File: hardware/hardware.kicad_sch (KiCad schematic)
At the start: 8 parts, among them J1 USB_C_Receptacle_USB2.0_14P, J2 Conn_01x04_Socket, J3 Conn_01x08_Socket, J4 Conn_01x04_Socket, U1 AMS1117-3.3, U2 ESP32-S3-WROOM-1

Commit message: Update Footprint property for connectors in schematic
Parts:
- J2, J4: footprint (none) -> Connector_PinHeader_2.54mm:PinHeader_1x04_P2.54mm_Vertical
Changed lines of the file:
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@@
 			)
 		)
-		(property "Footprint" ""
+		(property "Footprint" "Connector_PinHeader_2.54mm:PinHeader_1x04_P2.54mm_Vertical"
 			(at 200.66 24.13 0)
 			(effects
@@
 			)
 		)
-		(property "Footprint" ""
+		(property "Footprint" "Connector_PinHeader_2.54mm:PinHeader_1x04_P2.54mm_Vertical"
 			(at 252.73 24.13 0)
 			(effects

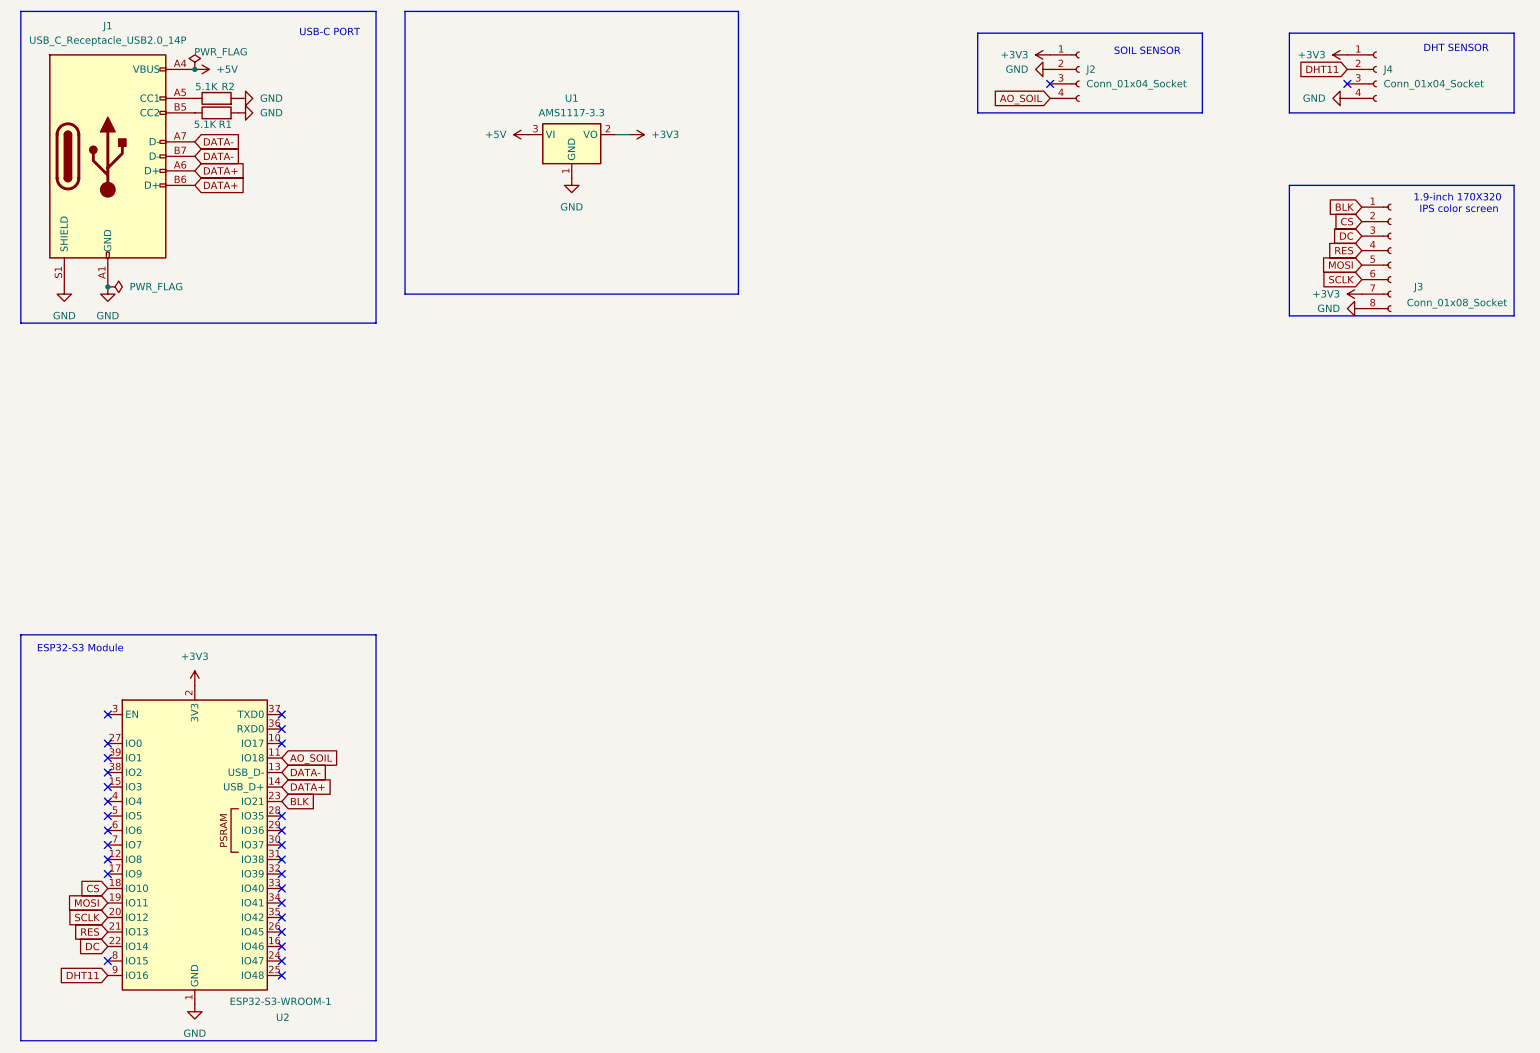
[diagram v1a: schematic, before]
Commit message: Adding Light sensor pins on schematic
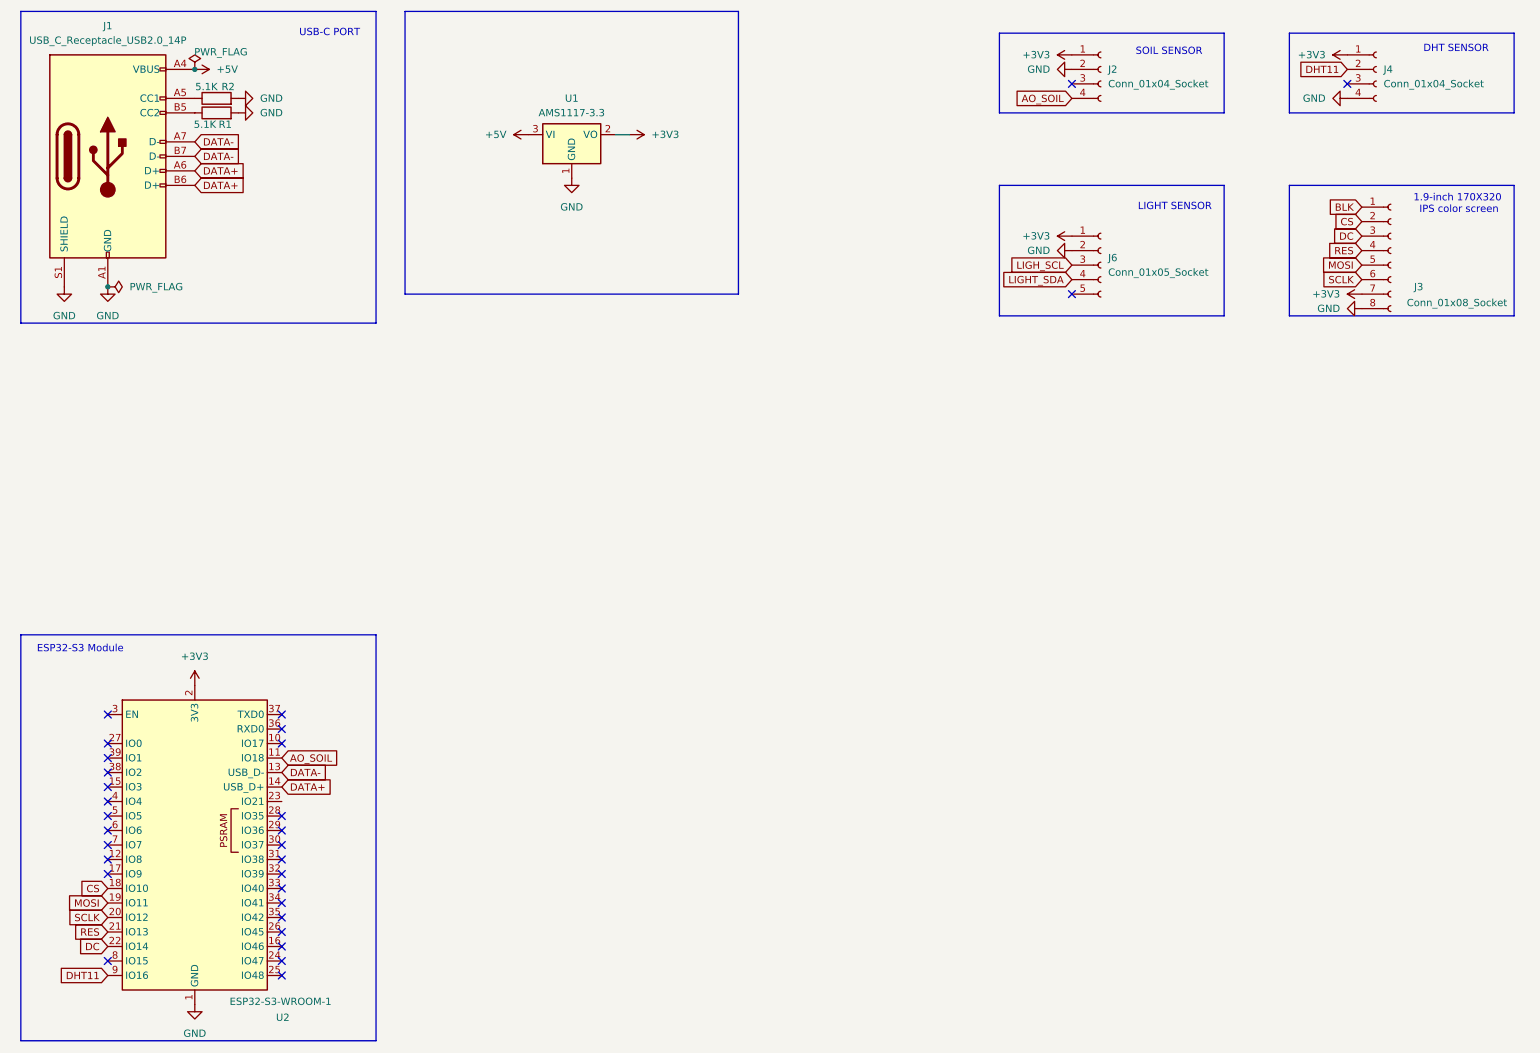
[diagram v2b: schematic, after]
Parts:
- added J6: Conn_01x05_Socket, symbol Connector:Conn_01x05_Socket
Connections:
- net +3V3: now also J6.1 (Pin_1)
- net BLK: no longer U2.23 (IO21)
- net GND: now also J6.2 (Pin_2)
- new net LIGHT_SDA: J6.4 (Pin_4)
- new net LIGH_SCL: J6.3 (Pin_3)
- no-connect marks 29 -> 30
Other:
- note added: "LIGHT SENSOR"
- moved on the sheet: J2

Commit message: Adding all capacitors
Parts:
- added C1, C2: 10uF, Capacitor_SMD:C_0805_2012Metric, symbol Device:C
- added C3, C6: 0.1uF, Capacitor_SMD:C_0805_2012Metric, symbol Device:C
- added C4, C7: 22uF, Capacitor_SMD:C_0805_2012Metric, symbol Device:C
- added C5: 10nF, Capacitor_SMD:C_0805_2012Metric, symbol Device:C
- J6: footprint (none) -> Connector_PinHeader_2.54mm:PinHeader_1x05_P2.54mm_Vertical
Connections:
- net +3V3: now also C1.2, C3.2, C4.1, C6.1, C7.1
- net +5V: now also C2.2, C5.1
- net GND: now also C1.1, C2.1, C3.1, C4.2, C5.2, C6.2, C7.2
- no-connect marks 30 -> 31
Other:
- note added: "sooit 22uF en ceramique soit 10uF en tantale"
- moved on the sheet: J1, J4, R1, R2

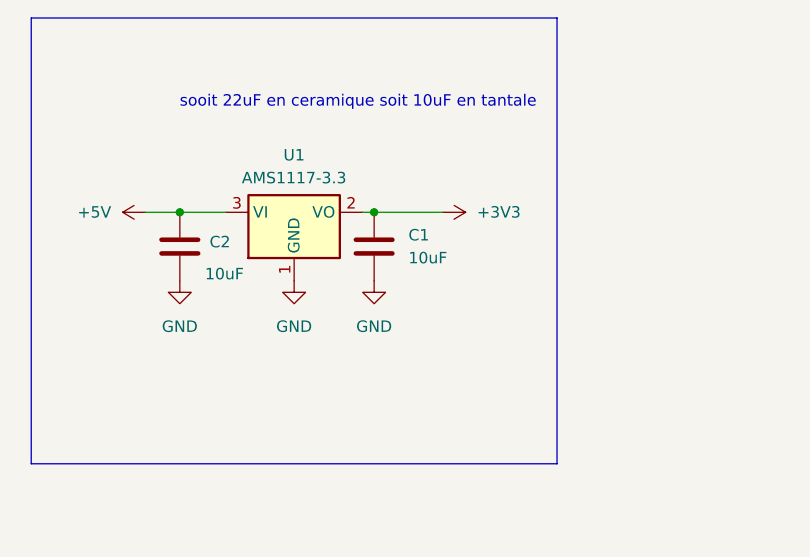
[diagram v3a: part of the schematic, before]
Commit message: Making first version of the PCB [NOT ROUTED ]
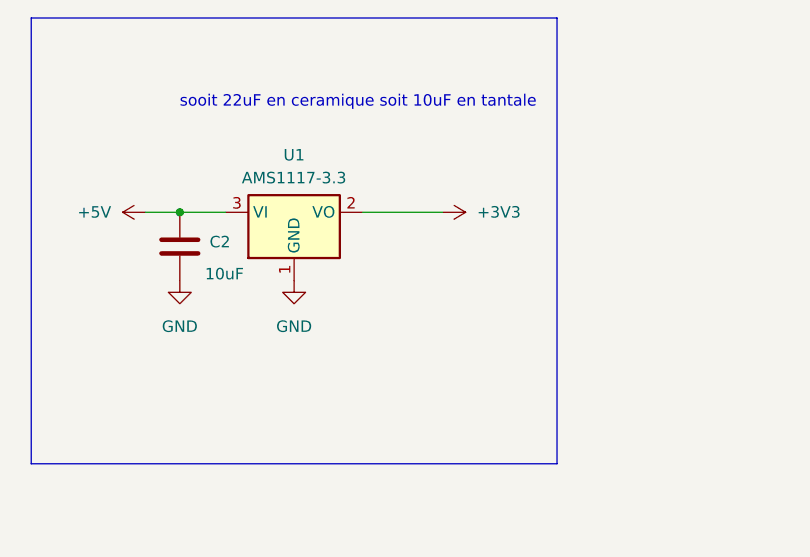
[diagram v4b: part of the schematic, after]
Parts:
- removed C1: 10uF, Capacitor_SMD:C_0805_2012Metric, symbol Device:C
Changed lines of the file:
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@@
-	)
-	(junction
-		(at 120.65 35.56)
-		(diameter 0)
-		(color 0 0 0 0)
 	)
 	(junction
@@
 	(wire
 		(pts
-			(xy 128.27 35.56) (xy 120.65 35.56)
+			(xy 55.88 29.21) (xy 46.99 29.21)
 		)
 		(stroke
@@
 	(wire
 		(pts
-			(xy 55.88 29.21) (xy 46.99 29.21)
+			(xy 45.72 130.81) (xy 45.72 132.08)
 		)
 		(stroke
@@
 	(wire
 		(pts
-			(xy 45.72 130.81) (xy 45.72 132.08)
-		)
-		(stroke
-			(width 0)
-			(type default)
-		)
-	)
-	(wire
-		(pts
-			(xy 120.65 35.56) (xy 119.38 35.56)
+			(xy 119.38 35.56) (xy 128.27 35.56)
 		)
 		(stroke
@@
 	)
 	(symbol
-		(lib_id "Device:C")
-		(at 120.65 39.37 180)
-		(unit 1)
-		(exclude_from_sim no)
-		(in_bom yes)
-		(on_board yes)
-		(dnp no)
-		(fields_autoplaced yes)
-		(property "Reference" "C1"
-			(at 124.46 38.0999 0)
-			(effects
-				(font
-					(size 1.27 1.27)
-				)
-				(justify right)
-			)
-		)
-		(property "Value" "10uF"
-			(at 124.46 40.6399 0)
-			(effects
-				(font
-					(size 1.27 1.27)
-				)
-				(justify right)
-			)
-		)
-		(property "Footprint" "Capacitor_SMD:C_0805_2012Metric"
-			(at 119.6848 35.56 0)
-			(effects
-				(font
-					(size 1.27 1.27)
-				)
-				(hide yes)
-			)
-		)
-		(property "Datasheet" "~"
-			(at 120.65 39.37 0)
-			(effects
-				(font
-					(size 1.27 1.27)
-				)
-				(hide yes)
-			)
-		)
-		(property "Description" "Unpolarized capacitor"
-			(at 120.65 39.37 0)
-			(effects
-				(font
-					(size 1.27 1.27)
-				)
-				(hide yes)
-			)
-		)
-		(pin "1"
-		)
-		(pin "2"
-		)
-		(instances
-			(project ""
-				(path "/a233d2e6-40a7-473a-8214-598adc2356c8"
-					(reference "C1")
-					(unit 1)
-				)
-			)
-		)
-	)
-	(symbol
 		(lib_id "power:GND")
 		(at 53.34 123.19 90)
@@
 					(unit 1)
 				)
-			)
-		)
-	)
-	(symbol
-		(lib_id "power:GND")
-		(at 120.65 43.18 0)
-		(unit 1)
-		(exclude_from_sim no)
-		(in_bom yes)
-		(on_board yes)
-		(dnp no)
-		(fields_autoplaced yes)
-		(property "Reference" "#PWR019"
-			(at 120.65 49.53 0)
-			(effects
-				(font
-					(size 1.27 1.27)
-				)
-				(hide yes)
-			)
-		)
-		(property "Value" "GND"
-			(at 120.65 48.26 0)
-			(effects
-				(font
-					(size 1.27 1.27)
-				)
-			)
-		)
-		(property "Footprint" ""
-			(at 120.65 43.18 0)
-			(effects
-				(font
-					(size 1.27 1.27)
-				)
-				(hide yes)
-			)
-		)
-		(property "Datasheet" ""
-			(at 120.65 43.18 0)
-			(effects
-				(font
-					(size 1.27 1.27)
-				)
-				(hide yes)
-			)
-		)
-		(property "Description" "Power symbol creates a global label with name \"GND\" , ground"
-			(at 120.65 43.18 0)
-			(effects
-				(font
-					(size 1.27 1.27)
-				)
-				(hide yes)
-			)
-		)
-		(pin "1"
-		)
-		(instances
-			(project "hardware"
-				(path "/a233d2e6-40a7-473a-8214-598adc2356c8"
-					(reference "#PWR019")
-					(unit 1)
-				)

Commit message: Removing message
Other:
- note removed: "sooit 22uF en ceramique soit 10uF en tantale"
- title: PlantMate -> FloraCare
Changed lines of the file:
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@@
 	(paper "A4")
 	(title_block
-		(title "PlantMate")
+		(title "FloraCare")
 		(date "2026-03-06")
 		(company "Trophées NSI")
@@
 		(effects
 			(font
-				(size 1.27 1.27)
-			)
-		)
-	)
-	(text "sooit 22uF en ceramique soit 10uF en tantale"
-		(exclude_from_sim no)
-		(at 118.872 23.368 0)
-		(effects
-			(font
